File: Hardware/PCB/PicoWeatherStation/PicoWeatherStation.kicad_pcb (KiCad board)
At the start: 2 copper layers, 109.2 x 67.3 mm, 40 parts, among them J1 TOUCH_PANEL, J2 LCD_BL, Q1 AO3400A, SW1 SW_PICO_RST, U1 Pico, U2 XPT2046, U3 nRF24L01+, U4 GY-BME280

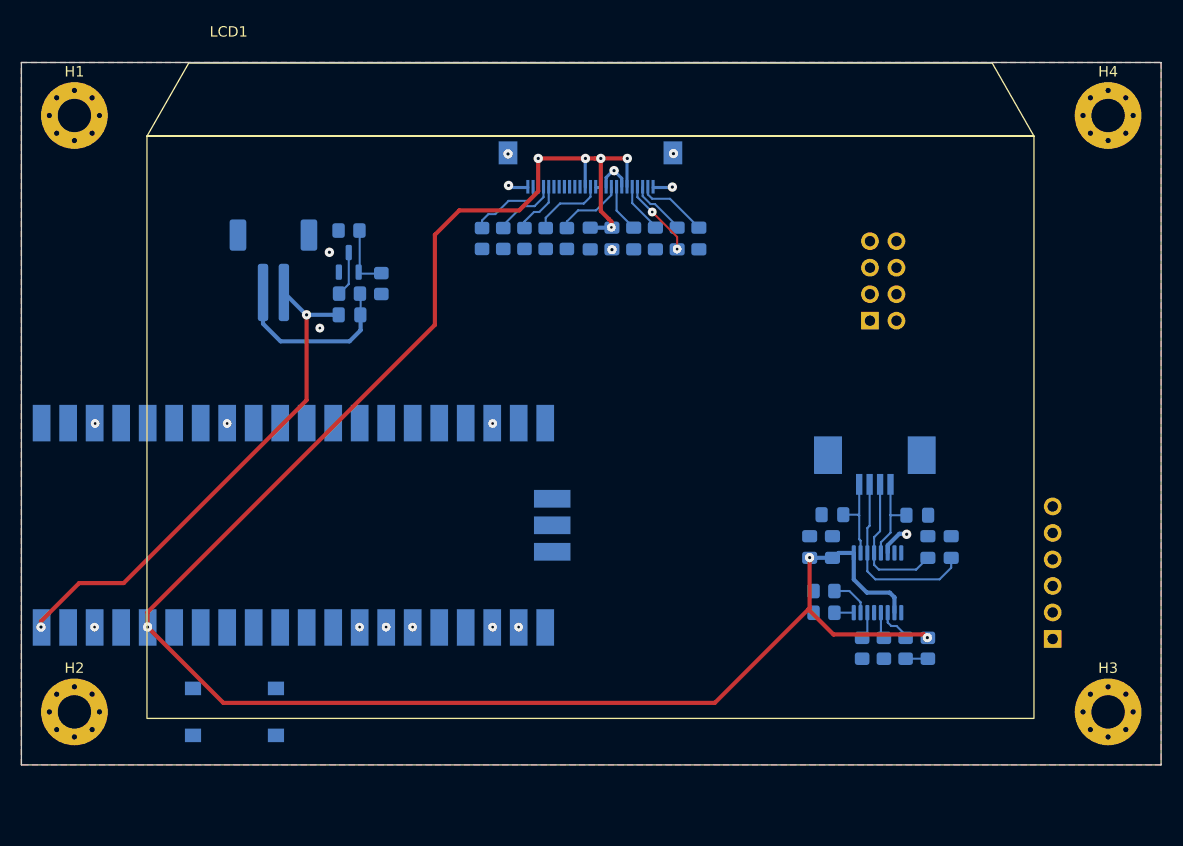
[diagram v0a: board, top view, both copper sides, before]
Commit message: Fully wire up the PCB
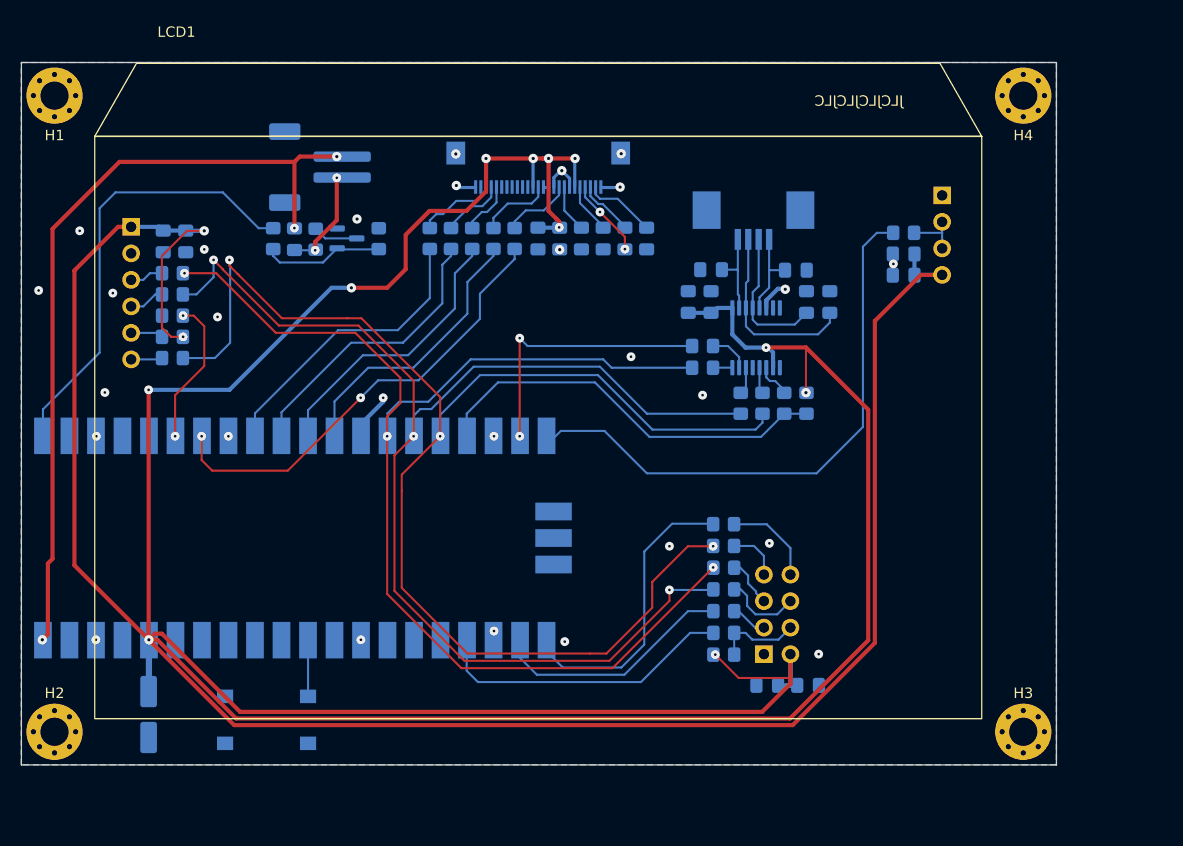
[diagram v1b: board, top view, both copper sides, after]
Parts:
- added C1: C_Polarized, Capacitor_SMD:CP_Elec_5x5.4, B.Cu at (94.7, 101.9)
- added C401: 1u, Capacitor_SMD:C_0805_2012Metric_Pad1.18x1.45mm_HandSolder, B.Cu at (154.0, 99.1)
- added C402: 100n, Capacitor_SMD:C_0805_2012Metric_Pad1.18x1.45mm_HandSolder, B.Cu at (157.9, 99.1)
- added C501: 1u, Capacitor_SMD:C_0805_2012Metric_Pad1.18x1.45mm_HandSolder, B.Cu at (96.1, 56.5)
- added C502: 100n, Capacitor_SMD:C_0805_2012Metric_Pad1.18x1.45mm_HandSolder, B.Cu at (98.3, 56.5)
- added C601: 1u, Capacitor_SMD:C_0805_2012Metric_Pad1.18x1.45mm_HandSolder, B.Cu at (167.1, 57.7)
- added C602: 100n, Capacitor_SMD:C_0805_2012Metric_Pad1.18x1.45mm_HandSolder, B.Cu at (167.1, 59.8)
- added R401: 100k, Resistor_SMD:R_0805_2012Metric_Pad1.20x1.40mm_HandSolder, B.Cu at (149.9, 96.1)
- added R402: 270, Resistor_SMD:R_0805_2012Metric_Pad1.20x1.40mm_HandSolder, B.Cu at (149.9, 91.9)
- added R403: 270, Resistor_SMD:R_0805_2012Metric_Pad1.20x1.40mm_HandSolder, B.Cu at (149.9, 94.0)
- added R404: 270, Resistor_SMD:R_0805_2012Metric_Pad1.20x1.40mm_HandSolder, B.Cu at (149.8, 83.6)
- added R405: 270, Resistor_SMD:R_0805_2012Metric_Pad1.20x1.40mm_HandSolder, B.Cu at (149.9, 89.9)
- added R406: 270, Resistor_SMD:R_0805_2012Metric_Pad1.20x1.40mm_HandSolder, B.Cu at (149.8, 85.7)
- added R407: 270, Resistor_SMD:R_0805_2012Metric_Pad1.20x1.40mm_HandSolder, B.Cu at (149.9, 87.8)
- added R501: 100k, Resistor_SMD:R_0805_2012Metric_Pad1.20x1.40mm_HandSolder, B.Cu at (97.0, 65.7)
- added R502: 270, Resistor_SMD:R_0805_2012Metric_Pad1.20x1.40mm_HandSolder, B.Cu at (97.0, 63.6)
- added R503: 270, Resistor_SMD:R_0805_2012Metric_Pad1.20x1.40mm_HandSolder, B.Cu at (97.0, 59.6)
- added R504: 270, Resistor_SMD:R_0805_2012Metric_Pad1.20x1.40mm_HandSolder, B.Cu at (97.0, 61.6)
- added R505: 270, Resistor_SMD:R_0805_2012Metric_Pad1.20x1.40mm_HandSolder, B.Cu at (97.0, 67.7)
- added R601: 270, Resistor_SMD:R_0805_2012Metric_Pad1.20x1.40mm_HandSolder, B.Cu at (167.1, 55.7)
- added U5: ZR-3A, PicoWeatherStation:ZR-3A, B.Cu at (175.5, 63.8)
- H1, H2, H3, H4: footprint MountingHole:MountingHole_3.2mm_M3_Pad_Via -> MountingHole:MountingHole_2.7mm_Pad_Via
- moved U4 101.0 mm to (88.5, 61.5), turned to -90 degrees
- moved U3 33.5 mm to (166.9, 89.9)
- moved R204 26.2 mm to (153.6, 72.0)
- moved R205 26.2 mm to (155.7, 72.0)
- moved R206 26.2 mm to (157.8, 72.0)
- moved U2 26.2 mm to (153.0, 65.8)
- moved C211 26.2 mm to (156.8, 59.3)
- moved C212 26.2 mm to (157.8, 62.3)
- moved C214 26.2 mm to (148.6, 59.2)
- moved J1 26.2 mm to (152.7, 54.5)
- moved R201 26.2 mm to (147.8, 68.6)
- moved R202 26.2 mm to (147.8, 66.5)
- moved R203 26.2 mm to (151.5, 72.0)
- moved C201 26.2 mm to (146.5, 62.3)
- moved C202 26.2 mm to (148.6, 62.3)
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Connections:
- R201 pad 2: TOUCH_DCLK -> SPI_PERI_SCK
- R203 pad 2: TOUCH_DIN -> SPI_PERI_MOSI
- R204 pad 2: TOUCH_DOUT -> SPI_PERI_MISO
- U1 pad 1: unconnected-(U1-Pad1) -> LCD_BL_PWM
- U1 pad 10: unconnected-(U1-Pad10) -> LCD_SDI
- U1 pad 11: unconnected-(U1-Pad11) -> LCD_D~{C}
- U1 pad 12: unconnected-(U1-Pad12) -> LCD_~{RST}
- U1 pad 14: unconnected-(U1-Pad14) -> SPI_PERI_SCK
- U1 pad 15: unconnected-(U1-Pad15) -> SPI_PERI_MOSI
- U1 pad 16: unconnected-(U1-Pad16) -> SPI_PERI_MISO
- U1 pad 17: unconnected-(U1-Pad17) -> TOUCH_~{PENIRQ}
- U1 pad 19: unconnected-(U1-Pad19) -> TOUCH_~{CS}
- U1 pad 20: unconnected-(U1-Pad20) -> ZR_OUT
- U1 pad 21: unconnected-(U1-Pad21) -> NRF_IRQ
- U1 pad 22: LCD_~{CS} -> NRF_CE
- U1 pad 24: LCD_SCK -> NRF_~{CSN}
- U1 pad 25: LCD_SDI -> unconnected-(U1-Pad25)
- U1 pad 26: LCD_~{RST} -> unconnected-(U1-Pad26)
- U1 pad 27: LCD_D~{C} -> unconnected-(U1-Pad27)
- U1 pad 6: unconnected-(U1-Pad6) -> BME_~{CSB}
- U1 pad 7: unconnected-(U1-Pad7) -> LCD_~{CS}
- U1 pad 9: unconnected-(U1-Pad9) -> LCD_SCK
- U3 pad 1: unconnected-(U3-Pad1) -> GND
- U3 pad 2: unconnected-(U3-Pad2) -> VDD
- U3 pad 3: unconnected-(U3-Pad3) -> Net-(R402-Pad2)
- U3 pad 4: unconnected-(U3-Pad4) -> Net-(R401-Pad2)
- U3 pad 5: unconnected-(U3-Pad5) -> Net-(R407-Pad1)
- U3 pad 6: unconnected-(U3-Pad6) -> Net-(R405-Pad1)
- U3 pad 7: unconnected-(U3-Pad7) -> Net-(R406-Pad1)
- U3 pad 8: unconnected-(U3-Pad8) -> Net-(R404-Pad2)
- U4 pad 1: unconnected-(U4-Pad1) -> VDD
- U4 pad 2: unconnected-(U4-Pad2) -> GND
- U4 pad 3: unconnected-(U4-Pad3) -> Net-(R503-Pad1)
- U4 pad 4: unconnected-(U4-Pad4) -> Net-(R504-Pad1)
- U4 pad 5: unconnected-(U4-Pad5) -> Net-(R502-Pad2)
- U4 pad 6: unconnected-(U4-Pad6) -> Net-(R505-Pad1)
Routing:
- net VDD: track 193.6 -> 498.2 mm, vias 8 -> 13
- net SPI_PERI_MISO: track 0.00 -> 135.7 mm, vias 0 -> 3
- net SPI_PERI_MOSI: track 0.00 -> 124.9 mm, vias 0 -> 3
- net SPI_PERI_SCK: track 0.00 -> 119.0 mm, vias 0 -> 3
- net ZR_OUT: track 0.00 -> 55.1 mm
- net LCD_BL_PWM: track 0.00 -> 43.6 mm
- net LCD_~{CS}: track 0.00 -> 43.5 mm, vias 1 -> 2
- net TOUCH_~{PENIRQ}: track 2.08 -> 39.9 mm
- net NRF_~{CSN}: track 0.00 -> 29.9 mm
- net NRF_IRQ: track 0.00 -> 29.6 mm
- net LCD_SCK: track 0.00 -> 29.1 mm
- net LCD_SDI: track 0.00 -> 28.5 mm
- net LCD_D~{C}: track 0.00 -> 27.9 mm, vias 1 -> 0
- net LCD_~{RST}: track 0.00 -> 27.7 mm, vias 1 -> 0
- net VBUS: track 49.1 -> 76.2 mm, vias 2 -> 3
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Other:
- board size 109.2 x 67.3 mm -> 99.2 x 67.3 mm
- board text added: "3V3"
- board text added: "ADC_VREF"
- board text added: "JLCJLCJLCJLC"

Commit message: Update the PCB
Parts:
- added R207: 270, Resistor_SMD:R_0805_2012Metric_Pad1.20x1.40mm_HandSolder, B.Cu at (151.5, 72.0)
- added SW2: SW_PICO_RST, Button_Switch_SMD:SW_Push_1P1T_NO_6x6mm_H9.5mm, F.Cu at (101.9, 107.4)
- added SW3: SW_PICO_RST, Button_Switch_SMD:SW_Push_1P1T_NO_6x6mm_H9.5mm, F.Cu at (112.9, 107.4)
- added SW4: SW_PICO_RST, Button_Switch_SMD:SW_Push_1P1T_NO_6x6mm_H9.5mm, F.Cu at (124.0, 107.4)
- added SW5: SW_PICO_RST, Button_Switch_SMD:SW_Push_1P1T_NO_6x6mm_H9.5mm, F.Cu at (135.1, 107.4)
- added SW6: SW_PICO_RST, Button_Switch_SMD:SW_Push_1P1T_NO_6x6mm_H9.5mm, F.Cu at (157.2, 107.4)
- added SW7: SW_PICO_RST, Button_Switch_SMD:SW_Push_1P1T_NO_6x6mm_H9.5mm, F.Cu at (146.2, 107.4)
- added U6: 47L16, Package_SO:SOIC-8_3.9x4.9mm_P1.27mm, B.Cu at (153.4, 101.7)
- added U7: MCP7940N-xSN, Package_SO:SOIC-8_3.9x4.9mm_P1.27mm, B.Cu at (166.9, 101.7)
- moved C401 4.19 mm to (154.0, 94.9)
- moved C402 4.19 mm to (157.9, 94.9)
- moved R401 4.19 mm to (149.9, 91.9)
- moved R403 4.19 mm to (149.9, 89.8)
- moved R404 4.19 mm to (149.8, 79.4)
- moved R405 4.19 mm to (149.9, 85.7)
- moved R406 4.19 mm to (149.8, 81.5)
- moved R407 4.19 mm to (149.9, 83.6)
- moved U3 4.19 mm to (166.9, 85.7)
- moved R402 4.19 mm to (149.9, 87.8)
- moved H2 2.67 mm to (85.7, 106.2)
- moved H3 2.67 mm to (178.6, 106.2)
- moved R203 2.01 mm to (149.5, 72.0)
- moved C601 1.65 mm to (167.1, 56.1)
- moved C602 1.65 mm to (167.1, 58.1)
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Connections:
- U1 pad 20: ZR_OUT -> TOUCH_BUSY
- U1 pad 25: unconnected-(U1-Pad25) -> ZR_OUT
- U2 pad 13: unconnected-(U2-Pad13) -> Net-(U2-Pad13)
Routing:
- net ZR_OUT: track 55.1 -> 92.3 mm
- net TOUCH_BUSY: track 0.00 -> 23.5 mm, vias 0 -> 3
- net VDD: track 498.2 -> 504.9 mm
- net NRF_CE: track 24.3 -> 29.8 mm
- net SPI_PERI_SCK: track 119.0 -> 124.0 mm
- net NRF_~{CSN}: track 29.9 -> 34.4 mm
- net SPI_PERI_MISO: track 135.7 -> 140.1 mm
- net NRF_IRQ: track 29.6 -> 33.8 mm
- net SPI_PERI_MOSI: track 124.9 -> 128.0 mm
- net Net-(U2-Pad13): track 0.00 -> 2.88 mm
- net Net-(R203-Pad1): track 2.62 -> 4.42 mm
- net VBUS: track 76.2 -> 77.6 mm
- net GND: vias 28 -> 54
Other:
- board size 99.2 x 67.3 mm -> 99.2 x 73 mm
- board text added: "CONN_LCD_BL"
- board text added: "RESET"
- board text added: "ZR_OUT"

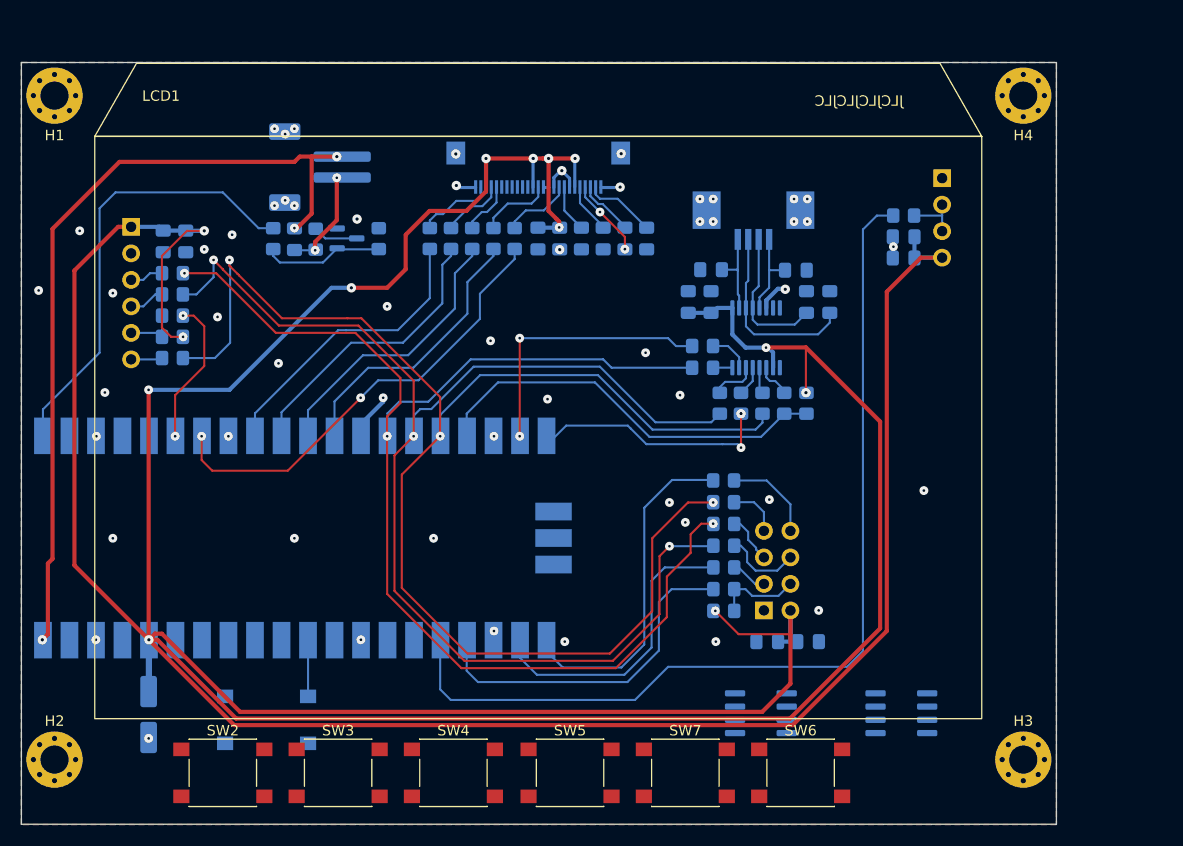
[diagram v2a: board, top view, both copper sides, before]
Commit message: PCB: add RTC and EERAM
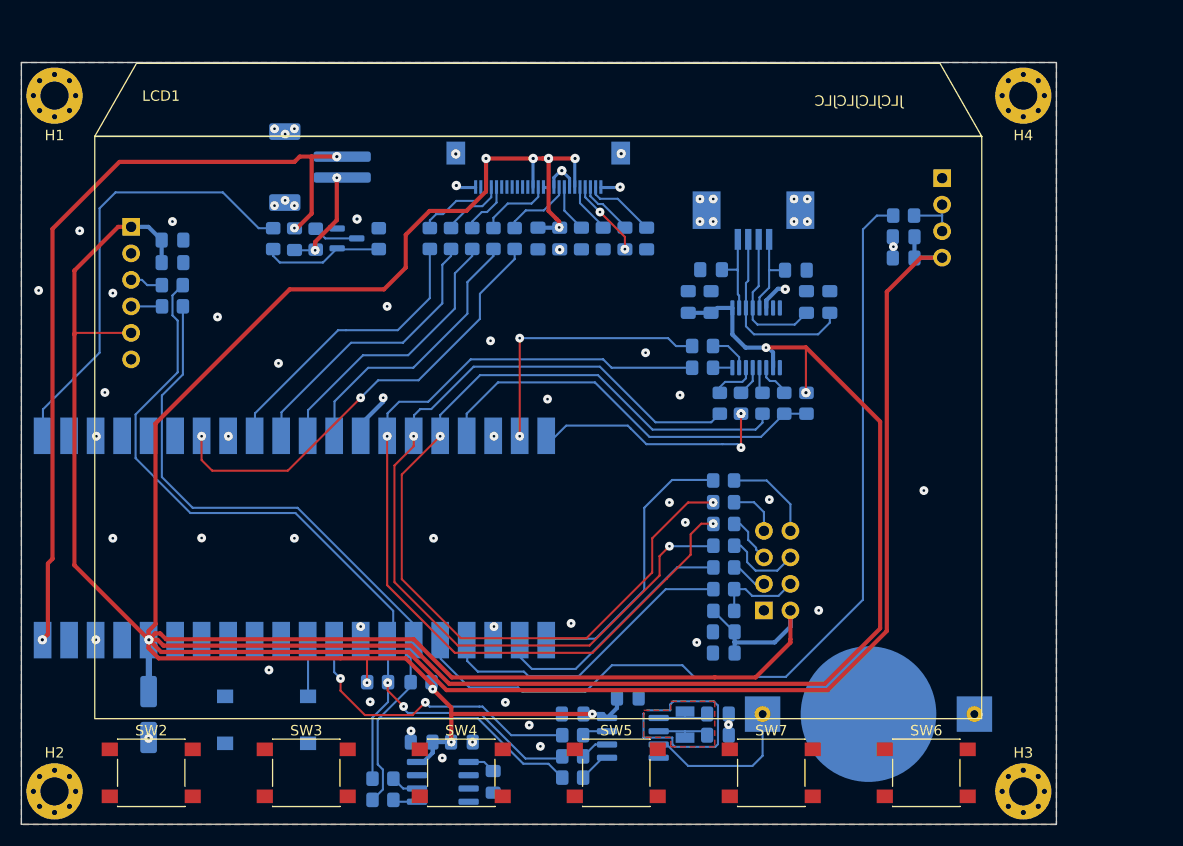
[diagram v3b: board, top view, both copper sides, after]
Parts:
- removed R503, R504, R505: 270, Resistor_SMD:R_0805_2012Metric_Pad1.20x1.40mm_HandSolder
- added BT1: CR1632, PicoWeatherStation:Battery_Holder_CR1632, B.Cu at (163.7, 101.8)
- added C701: 1u, Capacitor_SMD:C_0805_2012Metric_Pad1.18x1.45mm_HandSolder, B.Cu at (124.8, 104.5)
- added C702: 100n, Capacitor_SMD:C_0805_2012Metric_Pad1.18x1.45mm_HandSolder, B.Cu at (120.9, 104.5)
- added C703: 22u, Capacitor_SMD:C_0805_2012Metric_Pad1.18x1.45mm_HandSolder, B.Cu at (127.8, 108.3)
- added C801: 1u, Capacitor_SMD:C_0805_2012Metric_Pad1.18x1.45mm_HandSolder, B.Cu at (140.7, 100.3)
- added C802: 100n, Capacitor_SMD:C_0805_2012Metric_Pad1.18x1.45mm_HandSolder, B.Cu at (135.4, 101.8)
- added CX1: 10pF, Capacitor_SMD:C_0805_2012Metric_Pad1.18x1.45mm_HandSolder, B.Cu at (149.3, 101.8)
- added CX2: 12pF, Capacitor_SMD:C_0805_2012Metric_Pad1.18x1.45mm_HandSolder, B.Cu at (149.3, 103.8)
- added R1: 4k7, Resistor_SMD:R_0805_2012Metric_Pad1.20x1.40mm_HandSolder, B.Cu at (116.7, 98.8)
- added R2: 4k7, Resistor_SMD:R_0805_2012Metric_Pad1.20x1.40mm_HandSolder, B.Cu at (120.9, 98.8)
- added R701: 270, Resistor_SMD:R_0805_2012Metric_Pad1.20x1.40mm_HandSolder, B.Cu at (117.2, 108.0)
- added R702: 270, Resistor_SMD:R_0805_2012Metric_Pad1.20x1.40mm_HandSolder, B.Cu at (117.2, 110.0)
- added R801: 270, Resistor_SMD:R_0805_2012Metric_Pad1.20x1.40mm_HandSolder, B.Cu at (135.4, 105.9)
- added R802: 270, Resistor_SMD:R_0805_2012Metric_Pad1.20x1.40mm_HandSolder, B.Cu at (135.4, 107.9)
- added R803: 270, Resistor_SMD:R_0805_2012Metric_Pad1.20x1.40mm_HandSolder, B.Cu at (135.4, 103.8)
- added Y1: 32.768 kHz, 7 pF, 20 ppm, Crystal:Crystal_SMD_3215-2Pin_3.2x1.5mm, B.Cu at (146.1, 102.8)
- R501: value 100k -> 270
- U1: footprint RPi_Pico:RPi_Pico_SMD -> PicoWeatherStation:RPi_PicoW_SMD
- moved U6 31.2 mm to (122.9, 108.3)
- moved U7 25.8 mm to (141.1, 104.1)
- moved SW6 12.0 mm to (169.3, 107.4)
- moved SW7 8.24 mm to (154.4, 107.4)
- moved C402 8.15 mm to (149.9, 96.0), turned to 180 degrees
- moved SW2 6.86 mm to (95.0, 107.4)
- moved R501 4.95 mm to (97.0, 60.7), turned to 0 degrees
- moved SW5 4.43 mm to (139.6, 107.4)
- moved C401 4.27 mm to (149.9, 93.9)
- moved SW3 3.05 mm to (109.8, 107.4)
- moved H2 3.05 mm to (85.7, 109.2)
- moved H3 3.05 mm to (178.6, 109.2)
- moved C501 2.22 mm to (97.0, 58.5), turned to 0 degrees
- moved C502 1.28 mm to (97.0, 56.4), turned to 0 degrees
- moved R502 0.89 mm to (97.0, 62.7), turned to 0 degrees
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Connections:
- R501 pad 1: VDD -> Net-(R501-Pad1)
- R501 pad 2: Net-(R502-Pad2) -> I2C_SCL
- R502 pad 1: BME_~{CSB} -> Net-(R502-Pad1)
- R502 pad 2: Net-(R502-Pad2) -> I2C_SDA
- U1 pad 26: unconnected-(U1-Pad26) -> I2C_SDA
- U1 pad 27: unconnected-(U1-Pad27) -> I2C_SCL
- U1 pad 29: unconnected-(U1-Pad29) -> RTC_MFP
- U1 pad 6: BME_~{CSB} -> unconnected-(U1-Pad6)
- U4 pad 3: Net-(R503-Pad1) -> Net-(R501-Pad1)
- U4 pad 4: Net-(R504-Pad1) -> Net-(R502-Pad1)
- U4 pad 5: Net-(R502-Pad2) -> VDD
- U4 pad 6: Net-(R505-Pad1) -> GND
- U6 pad 1: unconnected-(U6-Pad1) -> Net-(C703-Pad1)
- U6 pad 4: unconnected-(U6-Pad4) -> GND
- U6 pad 5: unconnected-(U6-Pad5) -> Net-(R702-Pad2)
- U6 pad 6: unconnected-(U6-Pad6) -> Net-(R701-Pad2)
- U6 pad 8: unconnected-(U6-Pad8) -> VDD
- U7 pad 1: unconnected-(U7-Pad1) -> Net-(CX1-Pad1)
- U7 pad 2: unconnected-(U7-Pad2) -> Net-(CX2-Pad1)
- U7 pad 3: unconnected-(U7-Pad3) -> Net-(BT1-Pad1)
- U7 pad 4: unconnected-(U7-Pad4) -> GND
- U7 pad 5: unconnected-(U7-Pad5) -> Net-(R802-Pad2)
- U7 pad 6: unconnected-(U7-Pad6) -> Net-(R801-Pad2)
- U7 pad 7: unconnected-(U7-Pad7) -> Net-(R803-Pad2)
- U7 pad 8: unconnected-(U7-Pad8) -> VDD
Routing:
- net I2C_SCL: track 0.00 -> 86.7 mm, vias 0 -> 2
- net I2C_SDA: track 0.00 -> 86.5 mm
- net SPI_PERI_MISO: track 140.1 -> 93.4 mm, vias 3 -> 2
- net SPI_PERI_MOSI: track 128.0 -> 89.5 mm, vias 3 -> 2
- net VDD: track 504.9 -> 542.2 mm, vias 13 -> 12
- net SPI_PERI_SCK: track 124.0 -> 89.2 mm, vias 3 -> 2
- net RTC_MFP: track 0.00 -> 30.1 mm, vias 0 -> 2
- net GND: track 15.3 -> 37.0 mm, vias 54 -> 63
- net Net-(BT1-Pad1): track 0.00 -> 15.2 mm
- net BME_~{CSB}: track 14.2 -> 0.00 mm, vias 2 -> 0
- net Net-(CX2-Pad1): track 0.00 -> 5.43 mm
- net Net-(CX1-Pad1): track 0.00 -> 5.41 mm
- net Net-(R502-Pad2): track 5.15 -> 0.00 mm
- net NRF_IRQ: track 33.8 -> 29.2 mm
- net ZR_OUT: track 92.3 -> 88.0 mm
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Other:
- board text removed: "3V3"
- board text removed: "ADC_VREF"
